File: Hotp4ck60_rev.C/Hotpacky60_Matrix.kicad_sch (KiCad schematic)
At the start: 127 parts

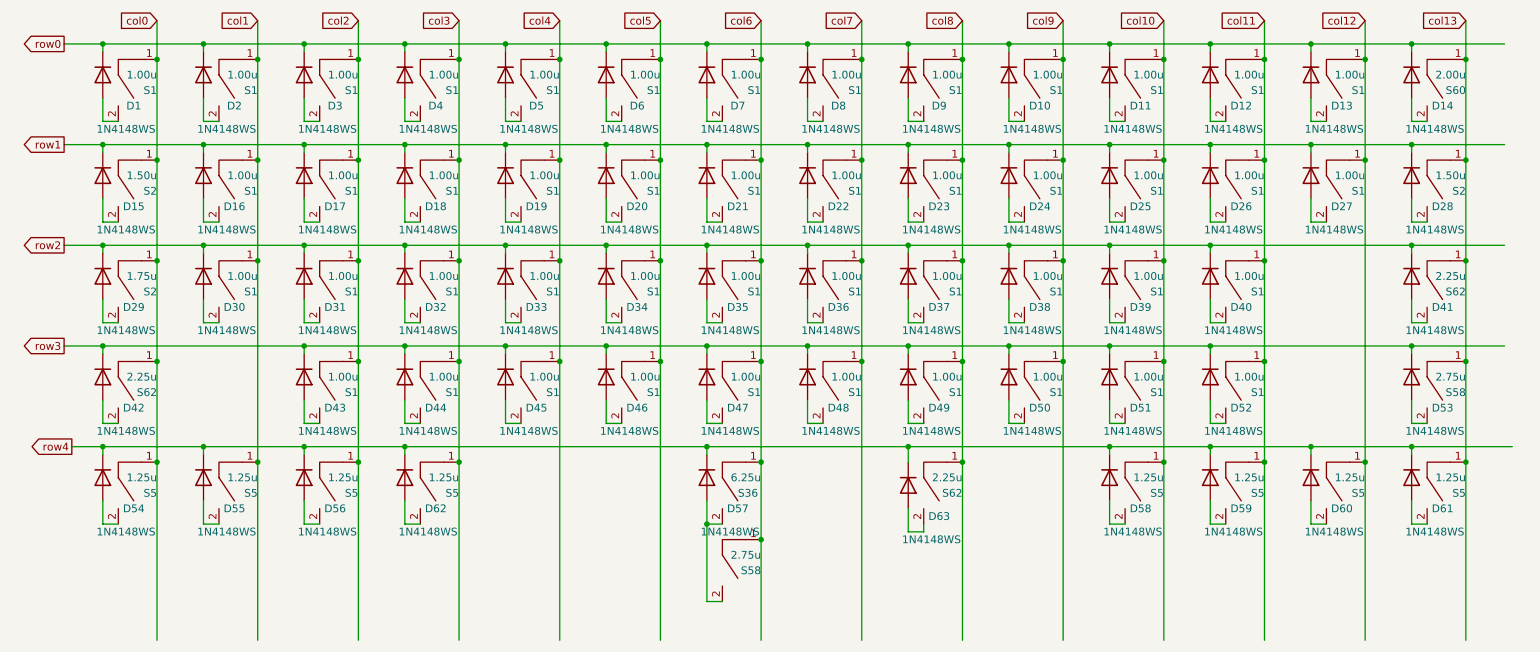
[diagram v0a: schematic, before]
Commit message: unified daughterboard, MCU 추가
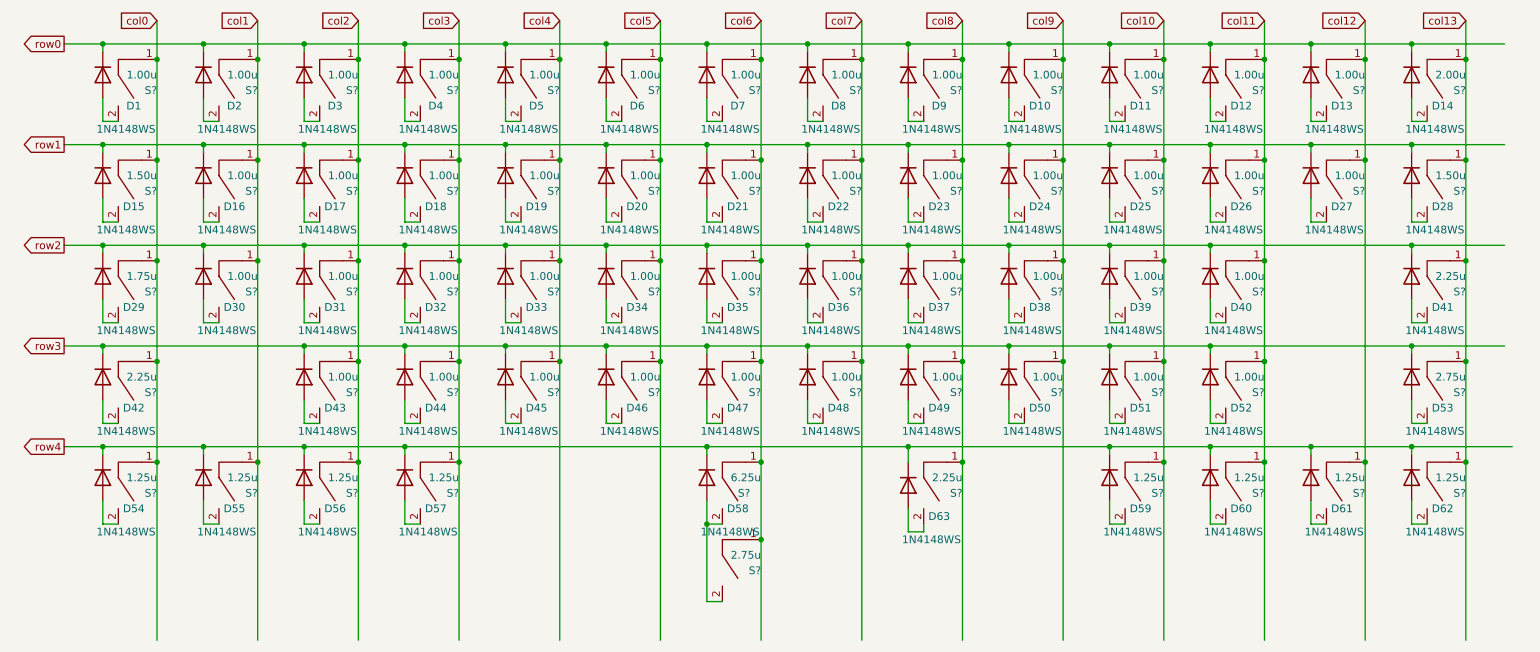
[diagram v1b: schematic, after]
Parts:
- renumbered D62 to D57, D57 to D58, D58 to D59, D59 to D60, D60 to D61, D61 to D62, S62 to S?, S1 to S?, S2 to S?, S5 to S?, S58 to S?, S36 to S?, S60 to S?

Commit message: README 수정
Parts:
- D1, D10, D11, D12, D13, D14, D15, D16, D17, D18, D19, D2, D20, D21, D22, D23, D24, D25, D26, D27, D28, D29, D3, D30, D31, D32, D33, D34, D35, D36, D37, D38, D39, D4, D40, D41, D42, D43, D44, D45, D46, D47, D48, D49, D5, D50, D51, D52, D53, D54, D55, D56, D57, D58, D59, D6, D60, D61, D62, D63, D7, D8, D9: LCSC (none) -> C2128

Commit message: rev.C neocore
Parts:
- removed S? (x45): 1.00u, Switch_Keyboard_Cherry_MX:SW_Cherry_MX_PCB_1.00u, symbol mx1a-simple:MX1A
- removed S? (x7): 1.25u, Switch_Keyboard_Cherry_MX:SW_Cherry_MX_PCB_1.25u, symbol mx1a-simple:MX1A
- removed S?: 2.00u, Switch_Keyboard_Cherry_MX:SW_Cherry_MX_PCB_2.00u, symbol mx1a-simple:MX1A
- removed S?: 1.50u, Switch_Keyboard_Cherry_MX:SW_Cherry_MX_PCB_1.50u, symbol mx1a-simple:MX1A
- added D53: 1N4148WS, Diode_SMD:D_SOD-323, symbol Diode:1N4148WS
- added S10, S11, S12, S13, S16, S17, S18, S19, S2, S20, S21, S22, S23, S24, S25, S26, S27, S3, S30, S31, S32, S33, S34, S35, S36, S37, S38, S39, S4, S40, S43, S44, S45, S46, S47, S48, S49, S5, S50, S51, S52, S54_1, S6, S7, S8, S9: 1.00u, Switch_Keyboard_Cherry_MX:SW_Cherry_MX_PCB_1.00u, symbol mx1a-simple:MX1A
- added S14: 2.00u, Switch_Keyboard_Cherry_MX:SW_Cherry_MX_PCB_2.00u, symbol mx1a-simple:MX1A
- added S28: 1.50u, Switch_Keyboard_Cherry_MX:SW_Cherry_MX_PCB_1.50u, symbol mx1a-simple:MX1A
- added S53: 1.75u, Switch_Keyboard_Cherry_MX:SW_Cherry_MX_PCB_1.75u, symbol mx1a-simple:MX1A
- added S56, S57, S58, S61, S62, S63, S64: 1.25u, Switch_Keyboard_Cherry_MX:SW_Cherry_MX_PCB_1.25u, symbol mx1a-simple:MX1A
- gave numbers to parts that had none: 10
- renumbered D53 to D54, D54 to D55, D55 to D56, D56 to D57, D57 to D58, D58 to D59, D63 to D60, D59 to D61, D60 to D62, D61 to D63, D62 to D64
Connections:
- net col0: now also S1.1
- net col1: now also S16.1, S2.1, S30.1, S56.1
- net col10: now also S11.1, S25.1, S39.1, S51.1, S61.1
- net col11: now also S12.1, S26.1, S40.1, S52.1, S62.1
- net col12: now also S13.1, S27.1, S53.1, S63.1
- net col13: now also S14.1, S28.1, S54_1.1, S64.1
- net col2: now also S17.1, S3.1, S31.1, S43.1, S57.1; no longer S1.1
- net col3: now also S18.1, S32.1, S4.1, S44.1, S58.1
- net col4: now also S19.1, S33.1, S45.1, S5.1
- net col5: now also S20.1, S34.1, S46.1, S6.1
- net col6: now also S21.1, S35.1, S47.1, S7.1
- net col7: now also S22.1, S36.1, S48.1, S8.1
- net col8: now also S23.1, S37.1, S49.1, S9.1
- net col9: now also S10.1, S24.1, S38.1, S50.1
- net row3: now also D53.1 (K)
- net at D56.2 (A): now also S56.2
- net at D64.2 (A): now also S64.2
- net at D57.2 (A): now also S57.2
- net at D25.2 (A): now also S25.2
- net at D2.2 (A): now also S2.2
- net at D27.2 (A): now also S27.2
- net at D45.2 (A): now also S45.2
- net at D36.2 (A): now also S36.2
- net at D63.2 (A): now also S63.2
- net at D23.2 (A): now also S23.2
- net at D14.2 (A): now also S14.2
- net at D8.2 (A): now also S8.2
- net at D35.2 (A): now also S35.2
- net at D26.2 (A): now also S26.2
- net at D52.2 (A): now also S52.2
- net at D5.2 (A): now also S5.2
- net at D46.2 (A): now also S46.2
- net at D50.2 (A): now also S50.2
- net at D43.2 (A): now also S43.2; no longer S1.2
- net at D34.2 (A): now also S34.2
- net at D6.2 (A): now also S6.2
- net at D38.2 (A): now also S38.2
- net at D32.2 (A): now also S32.2
- net at D4.2 (A): now also S4.2
- net at D11.2 (A): now also S11.2
- net at D62.2 (A): now also S62.2
- net at D51.2 (A): now also S51.2
- net at D3.2 (A): now also S3.2
- net at D21.2 (A): now also S21.2
- net at D30.2 (A): now also S30.2
- net at D49.2 (A): now also S49.2
- net at D39.2 (A): now also S39.2
- net at D33.2 (A): now also S33.2
- net at D13.2 (A): now also S13.2
- net at D48.2 (A): now also S48.2
- net at D54.2 (A), S54.2: now also S54_1.2
- net at D28.2 (A): now also S28.2
- net at D7.2 (A): now also S7.2
- net at D22.2 (A): now also S22.2
- net at D1.2 (A): now also S1.2
- net at D19.2 (A): now also S19.2
- net at D40.2 (A): now also S40.2
- net at D47.2 (A): now also S47.2
- net at D9.2 (A): now also S9.2
- net at D44.2 (A): now also S44.2
- net at D58.2 (A): now also S58.2
- net at D20.2 (A): now also S20.2
- net at D24.2 (A): now also S24.2
- net at D16.2 (A): now also S16.2
- net at D18.2 (A): now also S18.2
- net at D12.2 (A): now also S12.2
- net at D61.2 (A): now also S61.2
- net at D37.2 (A): now also S37.2
- net at D31.2 (A): now also S31.2
- net at D17.2 (A): now also S17.2
- net at D10.2 (A): now also S10.2
- new net: D53.2 (A), S53.2
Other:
- moved on the sheet: D1, D10, D11, D12, D13, D14, D15, D16, D17, D18, D19, D2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
